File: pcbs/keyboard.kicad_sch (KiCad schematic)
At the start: 160 parts, among them J1 MJ-4PP-9, J2 MJ-4PP-9, SW1 SW_PUSH, SW2 SW_PUSH, U1 Arduino_Pro_Micro, U2 Arduino_Pro_Micro

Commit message: Use smd+through hole diode footprint.
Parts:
- removed U1, U2: Arduino_Pro_Micro, ScottoKeebs_MCU:Arduino_Pro_Micro, symbol ScottoKeebs:MCU_Arduino_Pro_Micro
- added U1, U3: ProMicro, Corne:ProMicro_v3, symbol Corne:ProMicro
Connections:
- net GND: now also U3.23 (GND), U3.3 (GND), U3.4 (GND)
- net GNDA: now also U1.23 (GND), U1.3 (GND), U1.4 (GND)
- net VCC: now also U3.21 (VCC)
- net VDD: now also U1.21 (VCC)
- net col0: now also U3.13 (B6/10)
- net col0_r: now also U1.9 (6/D7)
- net col1_r: now also U1.8 (5/C6)
- net col2_r: now also U1.7 (4/D4)
- net col3_r: now also U1.13 (B6/10)
- net col4_r: now also U1.16 (B1/15)
- net col5_r: now also U1.17 (F7/A0)
- net col6_r: now also U1.18 (F6/A1)
- net col7_r: now also U1.19 (F5/A2)
- net data: now also U3.2 (RX1/D2)
- net data_r: now also U1.2 (RX1/D2)
- net reset: now also U3.22 (RST)
- net reset_r: now also U1.22 (RST)
- net row0: now also U3.7 (4/D4)
- net row0_r: now also U1.20 (F4/A3)
- net row1_r: now also U1.12 (9/B5)
- net row2_r: now also U1.11 (8/B4)
- net row3_r: now also U1.10 (7/E6)
- net row4_r: now also U1.14 (B2/16)
- net row5_r: now also U1.15 (B3/14)
- no-connect marks 6 -> 8
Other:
- moved on the sheet: J2, S1, S2, S3, S4, SW1, SW2

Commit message: Fixed board outlines + breakout pads.
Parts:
- added SW3: RotaryEncoder_Switch, Keebio-Parts:RotaryEncoder_Alps_EC11E-Switch_Vertical_H20mm, symbol Device:RotaryEncoder_Switch
- D_0, D_1, D_10, D_11, D_12, D_13, D_14, D_15, D_16, D_17, D_18, D_19, D_2, D_20, D_21, D_22, D_23, D_24, D_25, D_26, D_27, D_28, D_29, D_3, D_30, D_31, D_32, D_33, D_34, D_35, D_36, D_37, D_38, D_39, D_4, D_5, D_6, D_7, D_8, D_9: footprint Diode_SMD:D_SOD-123 -> Corne:D3_TH_SMD_v2
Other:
- moved on the sheet: D_0, D_1, D_10, D_11, D_12, D_13, D_14, D_15, D_16, D_17, D_18, D_19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

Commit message: Added CU fill and other stuff.
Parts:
- added D_75: D, Corne:D3_TH_SMD_v2, symbol Device:D_Small
- S2, S3: footprint PCM_marbastlib-mx:STAB_MX_P_2.75u -> PCM_marbastlib-mx:STAB_MX_P_2u
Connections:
- net GND: now also SW3.C
- net col0_r: now also U1.18 (F6/A1); no longer U1.9 (6/D7)
- net col1: now also SW3.S1, U3.14 (B2/16)
- net col1_r: now also U1.19 (F5/A2); no longer U1.8 (5/C6)
- net col2: now also U3.15 (B3/14)
- net col2_r: now also U1.20 (F4/A3); no longer U1.7 (4/D4)
- net col3: now also U3.16 (B1/15)
- net col3_r: now also U1.12 (9/B5); no longer U1.13 (B6/10)
- net col4: now also U3.17 (F7/A0)
- net col4_r: now also U1.11 (8/B4); no longer U1.16 (B1/15)
- net col5: now also U3.18 (F6/A1)
- net col5_r: now also U1.10 (7/E6); no longer U1.17 (F7/A0)
- net col6: now also U3.19 (F5/A2)
- net col6_r: now also U1.9 (6/D7); no longer U1.18 (F6/A1)
- net col7_r: now also U1.8 (5/C6); no longer U1.19 (F5/A2)
- net row0: now also D_75.1 (K)
- net row0_r: now also U1.7 (4/D4); no longer U1.20 (F4/A3)
- net row1_r: now also U1.13 (B6/10); no longer U1.12 (9/B5)
- net row2: now also U3.12 (9/B5)
- net row2_r: now also U1.14 (B2/16); no longer U1.11 (8/B4)
- net row3: now also U3.11 (8/B4)
- net row3_r: now also U1.15 (B3/14); no longer U1.10 (7/E6)
- net row4: now also U3.10 (7/E6)
- net row4_r: now also U1.16 (B1/15); no longer U1.14 (B2/16)
- net row5: now also U3.9 (6/D7)
- net row5_r: now also U1.17 (F7/A0); no longer U1.15 (B3/14)
- net row6: now also U3.8 (5/C6)
- net encA: now reaches SW3.A
- net encB: now reaches SW3.B
- net rotB: now reaches SW3.S2
- net rotB: now also D_75.2 (A)
- no-connect marks 8 -> 11
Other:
- moved on the sheet: SW3

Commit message: Added LEDs for underglow.
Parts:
- added LED1, LED10, LED11, LED12, LED2, LED3, LED4, LED5, LED6, LED7, LED8, LED9: WS2812B, LED_SMD:LED_WS2812B_PLCC4_5.0x5.0mm_P3.2mm, symbol LED:WS2812B
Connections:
- net GND: now also LED1.3 (VSS), LED2.3 (VSS), LED3.3 (VSS), LED4.3 (VSS), LED5.3 (VSS), LED6.3 (VSS)
- net GNDA: now also LED10.3 (VSS), LED11.3 (VSS), LED12.3 (VSS), LED7.3 (VSS), LED8.3 (VSS), LED9.3 (VSS)
- net VCC: now also LED1.1 (VDD), LED2.1 (VDD), LED3.1 (VDD), LED4.1 (VDD), LED5.1 (VDD), LED6.1 (VDD)
- net VDD: now also LED10.1 (VDD), LED11.1 (VDD), LED12.1 (VDD), LED7.1 (VDD), LED8.1 (VDD), LED9.1 (VDD)
- net LED: now reaches U3.1 (TX0/D3)
- net LED: now also LED5.4 (DIN)
- net LED_r: now reaches U1.1 (TX0/D3)
- net LED_r: now also LED11.4 (DIN)
- new net: LED10.2 (DOUT), LED12.4 (DIN)
- new net: LED7.2 (DOUT), LED8.4 (DIN)
- new net: LED7.4 (DIN), LED9.2 (DOUT)
- new net: LED1.4 (DIN), LED3.2 (DOUT)
- new net: LED3.4 (DIN), LED5.2 (DOUT)
- new net: LED2.2 (DOUT), LED4.4 (DIN)
- new net: LED1.2 (DOUT), LED2.4 (DIN)
- new net: LED10.4 (DIN), LED8.2 (DOUT)
- new net: LED11.2 (DOUT), LED9.4 (DIN)
- new net: LED4.2 (DOUT), LED6.4 (DIN)
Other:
- company: (none) -> www.fatotesa.se
- title: (none) -> Fatotesa Split Keyboard
- moved on the sheet: D_0, D_1, D_10, D_11, D_12, D_13, D_14, D_15, D_16, D_17, D_18, D_19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

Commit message: Use MX+Choc switch footprints.
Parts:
- K_0, K_1, K_10, K_11, K_12, K_13, K_14, K_15, K_16, K_17, K_18, K_19, K_2, K_20, K_21, K_22, K_23, K_24, K_25, K_26, K_27, K_28, K_29, K_3, K_30, K_31, K_32, K_33, K_34, K_35, K_4, K_5, K_6, K_7, K_8, K_9: footprint PCM_marbastlib-mx:SW_MX_1u -> kbd:CherryMX_Choc_1u
- K_11, K_33: footprint PCM_marbastlib-mx:SW_MX_1.5u -> kbd:CherryMX_Choc_1.5u
- K_17: footprint PCM_marbastlib-mx:SW_MX_1.75u -> kbd:CherryMX_Choc_1.75u
- K_21, K_23, K_30, K_31, K_32, K_36, K_37, K_38, K_39: footprint PCM_marbastlib-mx:SW_MX_1.25u -> kbd:CherryMX_Choc_1.25u

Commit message: Re-design the outline based on the PCB.
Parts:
- D_0, D_1, D_10, D_11, D_12, D_13, D_14, D_15, D_16, D_17, D_18, D_19, D_2, D_20, D_21, D_22, D_23, D_24, D_25, D_26, D_27, D_28, D_29, D_3, D_30, D_31, D_32, D_33, D_34, D_35, D_36, D_37, D_38, D_39, D_4, D_5, D_6, D_7, D_75, D_8, D_9: footprint Corne:D3_TH_SMD_v2 -> kbd:D3_TH
- K_0, K_1, K_10, K_11, K_12, K_13, K_14, K_15, K_16, K_17, K_18, K_19, K_2, K_20, K_21, K_22, K_23, K_24, K_25, K_26, K_27, K_28, K_29, K_3, K_30, K_31, K_32, K_33, K_34, K_35, K_4, K_5, K_6, K_7, K_8, K_9: footprint kbd:CherryMX_Choc_1u -> MX_Only:MXOnly-1U-NoLED
- K_11: footprint kbd:CherryMX_Choc_1.5u -> MX_Only:MXOnly-1.5U-NoLED
- K_17: footprint kbd:CherryMX_Choc_1.75u -> MX_Only:MXOnly-1.75U-NoLED
- K_21: footprint kbd:CherryMX_Choc_1.25u -> Button_Switch_Keyboard:SW_Cherry_MX_ISOEnter_PCB
- K_23, K_30, K_31, K_32, K_36, K_37, K_38, K_39: footprint kbd:CherryMX_Choc_1.25u -> MX_Only:MXOnly-1.25U-NoLED
- K_33: footprint kbd:CherryMX_Choc_1.5u -> MX_Only:MXOnly-1.75U-NoLED
- S2: footprint PCM_marbastlib-mx:STAB_MX_P_2u -> PCM_marbastlib-mx:STAB_MX_P_2.75u
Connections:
- net col0: now also U3.19 (F5/A2); no longer U3.13 (B6/10)
- net col0_r: now also U1.19 (F5/A2); no longer U1.18 (F6/A1)
- net col1: now also U3.18 (F6/A1); no longer U3.14 (B2/16)
- net col1_r: now also U1.18 (F6/A1); no longer U1.19 (F5/A2)
- net col2: now also U3.17 (F7/A0); no longer U3.15 (B3/14)
- net col2_r: now also U1.17 (F7/A0); no longer U1.20 (F4/A3)
- net col3_r: now also U1.16 (B1/15); no longer U1.12 (9/B5)
- net col4: now also U3.15 (B3/14); no longer U3.17 (F7/A0)
- net col4_r: now also U1.15 (B3/14); no longer U1.11 (8/B4)
- net col5: now also U3.14 (B2/16); no longer U3.18 (F6/A1)
- net col5_r: now also U1.7 (4/D4); no longer U1.10 (7/E6)
- net col6: now also U3.13 (B6/10); no longer U3.19 (F5/A2)
- net col6_r: now also U1.14 (B2/16); no longer U1.9 (6/D7)
- net row0_r: now also U1.12 (9/B5); no longer U1.7 (4/D4)
- net row1_r: now also U1.11 (8/B4); no longer U1.13 (B6/10)
- net row2: now also U3.8 (5/C6); no longer U3.12 (9/B5)
- net row2_r: now also U1.10 (7/E6); no longer U1.14 (B2/16)
- net row3: now also U3.9 (6/D7); no longer U3.11 (8/B4)
- net row3_r: now also U1.9 (6/D7); no longer U1.15 (B3/14)
- net row4_r: now also U1.20 (F4/A3); no longer U1.16 (B1/15)
- net row5: now also U3.11 (8/B4); no longer U3.9 (6/D7)
- net row5_r: now also U1.13 (B6/10); no longer U1.17 (F7/A0)
- net row6: now also U3.12 (9/B5); no longer U3.8 (5/C6)

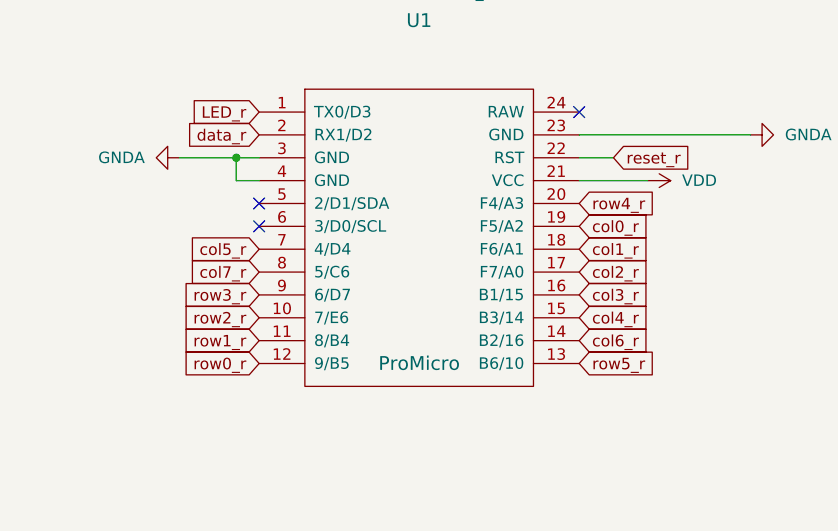
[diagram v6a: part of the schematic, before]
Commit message: Re-done traces.
After doing some more research, I've learned that power delivery traces
should be at least 0.5mm. I made them 1mm thick, and had to re-do all
traces.
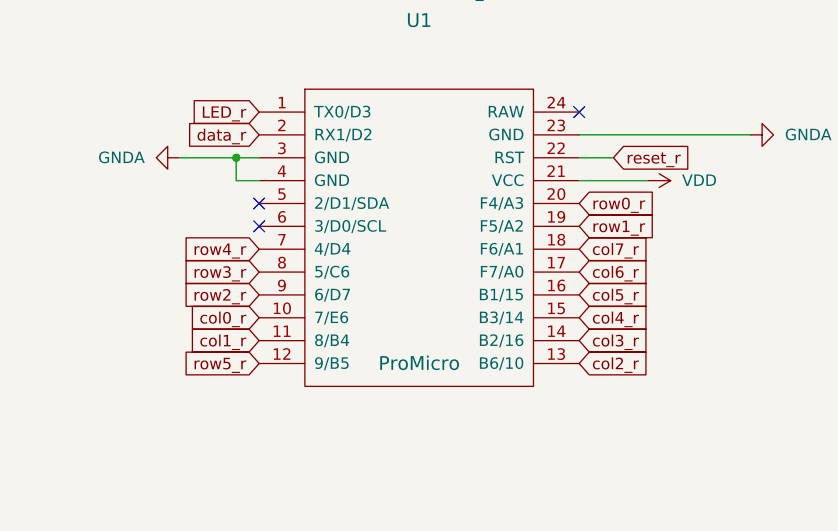
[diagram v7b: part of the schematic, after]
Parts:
- SW1, SW2: footprint Corne:ResetSW_1side -> kbd:ResetSMD_SG
- U1, U3: footprint Corne:ProMicro_v3 -> Corne:ProMicro_v3_inverted
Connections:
- net col0_r: now also U1.10 (7/E6); no longer U1.19 (F5/A2)
- net col1_r: now also U1.11 (8/B4); no longer U1.18 (F6/A1)
- net col2_r: now also U1.13 (B6/10); no longer U1.17 (F7/A0)
- net col3_r: now also U1.14 (B2/16); no longer U1.16 (B1/15)
- net col5_r: now also U1.16 (B1/15); no longer U1.7 (4/D4)
- net col6_r: now also U1.17 (F7/A0); no longer U1.14 (B2/16)
- net col7_r: now also U1.18 (F6/A1); no longer U1.8 (5/C6)
- net row0_r: now also U1.20 (F4/A3); no longer U1.12 (9/B5)
- net row1_r: now also U1.19 (F5/A2); no longer U1.11 (8/B4)
- net row2_r: now also U1.9 (6/D7); no longer U1.10 (7/E6)
- net row3_r: now also U1.8 (5/C6); no longer U1.9 (6/D7)
- net row4_r: now also U1.7 (4/D4); no longer U1.20 (F4/A3)
- net row5_r: now also U1.12 (9/B5); no longer U1.13 (B6/10)
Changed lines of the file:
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@@
     )
   )
-  (global_label "col3_r" (shape input) (at 447.675 379.73 0)
+  (global_label "col3_r" (shape input) (at 447.675 384.81 0)
     (effects (font (size 1.27 1.27)) (justify left))
-    (property "Intersheetrefs" "${INTERSHEET_REFS}" (at 447.675 379.73 0)
+    (property "Intersheetrefs" "${INTERSHEET_REFS}" (at 447.675 384.81 0)
       (effects (font (size 1.27 1.27)) hide)
     )
@@
     )
   )
-  (global_label "row0_r" (shape input) (at 412.115 387.35 180)
-    (effects (font (size 1.27 1.27)) (justify right))
-    (property "Intersheetrefs" "${INTERSHEET_REFS}" (at 412.115 387.35 0)
+  (global_label "row0_r" (shape input) (at 447.675 369.57 0)
+    (effects (font (size 1.27 1.27)) (justify left))
+    (property "Intersheetrefs" "${INTERSHEET_REFS}" (at 447.675 369.57 0)
       (effects (font (size 1.27 1.27)) hide)
     )
@@
     )
   )
-  (global_label "row5_r" (shape input) (at 447.675 387.35 0)
-    (effects (font (size 1.27 1.27)) (justify left))
-    (property "Intersheetrefs" "${INTERSHEET_REFS}" (at 447.675 387.35 0)
+  (global_label "row5_r" (shape input) (at 412.115 387.35 180)
+    (effects (font (size 1.27 1.27)) (justify right))
+    (property "Intersheetrefs" "${INTERSHEET_REFS}" (at 412.115 387.35 0)
       (effects (font (size 1.27 1.27)) hide)
     )
   )
-  (global_label "row4_r" (shape input) (at 447.675 369.57 0)
-    (effects (font (size 1.27 1.27)) (justify left))
-    (property "Intersheetrefs" "${INTERSHEET_REFS}" (at 447.675 369.57 0)
+  (global_label "row4_r" (shape input) (at 412.115 374.65 180)
+    (effects (font (size 1.27 1.27)) (justify right))
+    (property "Intersheetrefs" "${INTERSHEET_REFS}" (at 412.115 374.65 0)
       (effects (font (size 1.27 1.27)) hide)
     )
@@
     )
   )
-  (global_label "row2_r" (shape input) (at 412.115 382.27 180)
+  (global_label "row2_r" (shape input) (at 412.115 379.73 180)
     (effects (font (size 1.27 1.27)) (justify right))
-    (property "Intersheetrefs" "${INTERSHEET_REFS}" (at 412.115 382.27 0)
+    (property "Intersheetrefs" "${INTERSHEET_REFS}" (at 412.115 379.73 0)
       (effects (font (size 1.27 1.27)) hide)
     )
@@
     )
   )
-  (global_label "col1_r" (shape input) (at 447.675 374.65 0)
-    (effects (font (size 1.27 1.27)) (justify left))
-    (property "Intersheetrefs" "${INTERSHEET_REFS}" (at 447.675 374.65 0)
+  (global_label "col1_r" (shape input) (at 412.115 384.81 180)
+    (effects (font (size 1.27 1.27)) (justify right))
+    (property "Intersheetrefs" "${INTERSHEET_REFS}" (at 412.115 384.81 0)
       (effects (font (size 1.27 1.27)) hide)
     )
   )
-  (global_label "col6_r" (shape input) (at 447.675 384.81 0)
+  (global_label "col6_r" (shape input) (at 447.675 377.19 0)
     (effects (font (size 1.27 1.27)) (justify left))
-    (property "Intersheetrefs" "${INTERSHEET_REFS}" (at 447.675 384.81 0)
+    (property "Intersheetrefs" "${INTERSHEET_REFS}" (at 447.675 377.19 0)
       (effects (font (size 1.27 1.27)) hide)
     )
@@
     )
   )
-  (global_label "col2_r" (shape input) (at 447.675 377.19 0)
+  (global_label "col2_r" (shape input) (at 447.675 387.35 0)
     (effects (font (size 1.27 1.27)) (justify left))
-    (property "Intersheetrefs" "${INTERSHEET_REFS}" (at 447.675 377.19 0)
+    (property "Intersheetrefs" "${INTERSHEET_REFS}" (at 447.675 387.35 0)
       (effects (font (size 1.27 1.27)) hide)
     )
@@
     )
   )
-  (global_label "row3_r" (shape input) (at 412.115 379.73 180)
+  (global_label "row3_r" (shape input) (at 412.115 377.19 180)
     (effects (font (size 1.27 1.27)) (justify right))
-    (property "Intersheetrefs" "${INTERSHEET_REFS}" (at 412.115 379.73 0)
+    (property "Intersheetrefs" "${INTERSHEET_REFS}" (at 412.115 377.19 0)
       (effects (font (size 1.27 1.27)) hide)
     )
@@
     )
   )
-  (global_label "col5_r" (shape input) (at 412.115 374.65 180)
-    (effects (font (size 1.27 1.27)) (justify right))
-    (property "Intersheetrefs" "${INTERSHEET_REFS}" (at 412.115 374.65 0)
+  (global_label "col5_r" (shape input) (at 447.675 379.73 0)
+    (effects (font (size 1.27 1.27)) (justify left))
+    (property "Intersheetrefs" "${INTERSHEET_REFS}" (at 447.675 379.73 0)
       (effects (font (size 1.27 1.27)) hide)
     )
@@
     )
   )
-  (global_label "col0_r" (shape input) (at 447.675 372.11 0)
-    (effects (font (size 1.27 1.27)) (justify left))
-    (property "Intersheetrefs" "${INTERSHEET_REFS}" (at 447.675 372.11 0)
+  (global_label "col0_r" (shape input) (at 412.115 382.27 180)
+    (effects (font (size 1.27 1.27)) (justify right))
+    (property "Intersheetrefs" "${INTERSHEET_REFS}" (at 412.115 382.27 0)
       (effects (font (size 1.27 1.27)) hide)
     )
@@
     )
   )
-  (global_label "row1_r" (shape input) (at 412.115 384.81 180)
-    (effects (font (size 1.27 1.27)) (justify right))
-    (property "Intersheetrefs" "${INTERSHEET_REFS}" (at 412.115 384.81 0)
+  (global_label "row1_r" (shape input) (at 447.675 372.11 0)
+    (effects (font (size 1.27 1.27)) (justify left))
+    (property "Intersheetrefs" "${INTERSHEET_REFS}" (at 447.675 372.11 0)
       (effects (font (size 1.27 1.27)) hide)
     )
@@
     )
   )
-  (global_label "col7_r" (shape input) (at 412.115 377.19 180)
-    (effects (font (size 1.27 1.27)) (justify right))
-    (property "Intersheetrefs" "${INTERSHEET_REFS}" (at 412.115 377.19 0)
+  (global_label "col7_r" (shape input) (at 447.675 374.65 0)
+    (effects (font (size 1.27 1.27)) (justify left))
+    (property "Intersheetrefs" "${INTERSHEET_REFS}" (at 447.675 374.65 0)
       (effects (font (size 1.27 1.27)) hide)
     )
@@
       (effects (font (size 1.524 1.524)))
     )
-    (property "Footprint" "Corne:ProMicro_v3" (at 114.935 407.67 0)
+    (property "Footprint" "Corne:ProMicro_v3_inverted" (at 114.935 407.67 0)
       (effects (font (size 1.524 1.524)) hide)
     )
@@
       (effects (font (size 1.27 1.27)))
     )
-    (property "Footprint" "Corne:ResetSW_1side" (at 65.405 389.89 0)
+    (property "Footprint" "kbd:ResetSMD_SG" (at 65.405 389.89 0)
       (effects (font (size 1.27 1.27)) hide)
     )
@@
       (effects (font (size 1.524 1.524)))
     )
-    (property "Footprint" "Corne:ProMicro_v3" (at 432.435 400.05 0)
+    (property "Footprint" "Corne:ProMicro_v3_inverted" (at 432.435 400.05 0)
       (effects (font (size 1.524 1.524)) hide)
     )
@@
       (effects (font (size 1.27 1.27)))
     )
-    (property "Footprint" "Corne:ResetSW_1side" (at 363.855 361.95 0)
+    (property "Footprint" "kbd:ResetSMD_SG" (at 363.855 361.95 0)
       (effects (font (size 1.27 1.27)) hide)
     )

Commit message: Final touches, and the order.
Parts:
- added H1, H10, H11, H12, H13, H14, H15, H16, H17, H18, H19, H2, H20, H21, H22, H23, H24, H3, H4, H5, H6, H7, H8, H9: MountingHole, MountingHole:MountingHole_4.3mm_M4, symbol Mechanical:MountingHole
- added H25, H26, H27, H28, H29, H30, H31, H32: MountingHole, MountingHole:MountingHole_5.3mm_M5, symbol Mechanical:MountingHole
- added H33, H34, H35, H36, H37, H38, H39, H40: MountingHole, Keebio-Parts:breakaway-mousebites_fat-o-tesa, symbol Mechanical:MountingHole
